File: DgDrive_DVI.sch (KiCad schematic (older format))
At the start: 42 parts, among them J1 Curr. Mod., J2 DVI-I, J3 Ld+, J4 Ld-, J5 Pz+, J6 Pz-, J7 Piezo_In, K1 G6AU, Q1 MMBT3904, Q2 2N4401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

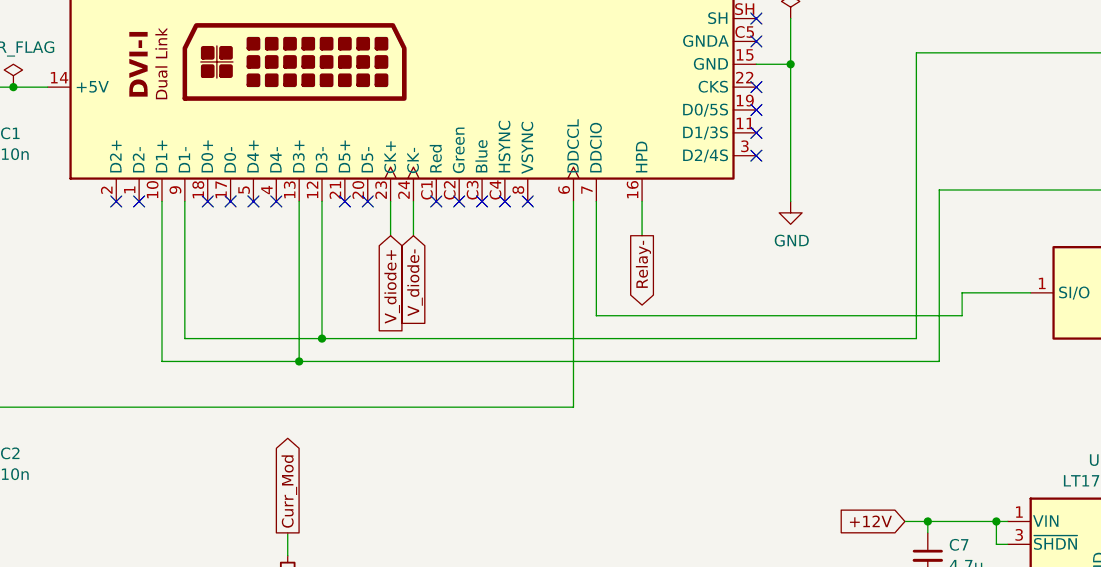
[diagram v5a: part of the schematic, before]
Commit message: Fix laser diode polarity
Switch LD-/LD+ pins at the DVI connector
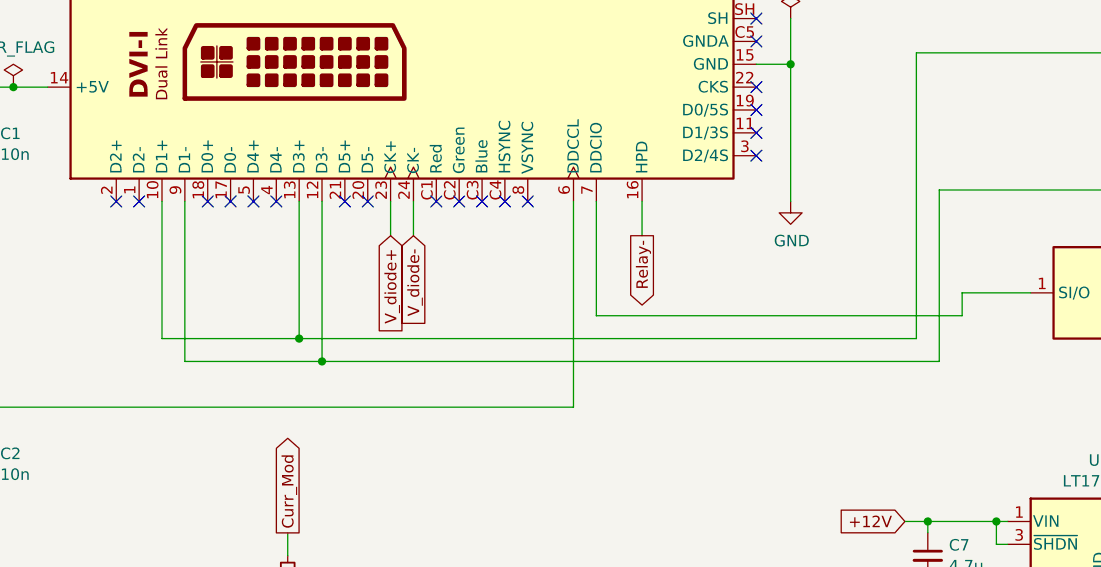
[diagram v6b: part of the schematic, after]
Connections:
- net at J2.10 (D1+), J2.13 (D3+): now also L1.1, R1.2; no longer L2.1, R6.2
- net at J2.12 (D3-), J2.9 (D1-): now also L2.1, R6.2; no longer L1.1, R1.2
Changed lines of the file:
@@
 Sheet 1 1
 Title "Laser Backplane Diode DVI"
-Date "2021-03-15"
-Rev "1.4"
+Date "2021-07-23"
+Rev "1.5"
 Comp "APQ"
 Comment1 "Tilman Preuschoff & Patrick Baus"
@@
 	8650 4200 8650 4100
 Connection ~ 8650 4100
-Wire Wire Line
-	2650 4150 2650 4850
-Wire Wire Line
-	2650 4850 3250 4850
-Wire Wire Line
-	3250 4150 3250 4850
-Connection ~ 3250 4850
-Wire Wire Line
-	2750 4150 2750 4750
-Wire Wire Line
-	2750 4750 3350 4750
-Wire Wire Line
-	3350 4150 3350 4750
-Connection ~ 3350 4750
 NoConn ~ 2450 4150
 NoConn ~ 2550 4150
@@
 	5950 4750 5950 3500
 Wire Wire Line
-	3350 4750 5950 4750
-Wire Wire Line
 	5950 3500 7700 3500
 Wire Wire Line
 	6050 4850 6050 4100
-Wire Wire Line
-	3250 4850 6050 4850
 Wire Wire Line
 	6050 4100 7700 4100
@@
 	1    0    0    1
 $EndComp
+Wire Wire Line
+	3250 4150 3250 4750
+Connection ~ 3250 4750
+Wire Wire Line
+	3250 4750 5950 4750
+Wire Wire Line
+	3350 4150 3350 4850
+Connection ~ 3350 4850
+Wire Wire Line
+	3350 4850 6050 4850
+Wire Wire Line
+	2650 4150 2650 4750
+Wire Wire Line
+	2650 4750 3250 4750
+Wire Wire Line
+	2750 4150 2750 4850
+Wire Wire Line
+	2750 4850 3350 4850
 $EndSCHEMATC

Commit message: Replace XGL3530 with XGL5050
-Use a larger inductance
-Options for no inductance at LD- and ground referenced design.
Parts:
- added JP1: No_L, Jumper:SolderJumper-2_P1.3mm_Open_RoundedPad1.0x1.5mm, symbol Device:Jumper_NO_Small
- added JP2: GND, Jumper:SolderJumper-2_P1.3mm_Open_RoundedPad1.0x1.5mm, symbol Device:Jumper_NO_Small
- C4: MFN (none) -> Yageo; PN (none) -> CC0603CPNPO9BN1R5
- L1: value 3.3u -> 33u; footprint custom:Coilcraft_XGL3530 -> custom:Coilcraft_XGL5050; PN XGL3530-332MEC -> XGL5050-333MEC
- L2: value 3.3u -> 33u; footprint custom:Coilcraft_XGL3530 -> custom:Coilcraft_XGL5050; PN XGL3530-332MEC -> XGL3530-333MEC
- R1, R6: MFN (none) -> Susumu; PN (none) -> RR0816Q-49R9-D-68R
- R4: MFN (none) -> Susumu; PN (none) -> RR0816Q-100-D
- RN1: value 10k -> 1k; PN MORNTA1002AT5 -> MORNTA1001AT5
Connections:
- net GND: now also JP2.2
- net LD_short-: now also JP1.1, JP2.1
- net at J2.12 (D3-), J2.9 (D1-), L2.1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: now also JP1.2
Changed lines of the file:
@@
 F 2 "Resistor_SMD:R_0603_1608Metric" H 8050 3500 50  0001 C CNN
 F 3 "~" H 8050 3500 50  0001 C CNN
-F 4 "" V 8050 3500 50  0001 C CNN "MFN"
-F 5 "" V 8050 3500 50  0001 C CNN "MFP"
+F 4 "Susumu" V 8050 3500 50  0001 C CNN "MFN"
+F 5 "RR0816Q-49R9-D-68R" V 8050 3500 50  0001 C CNN "PN"
 	1    8050 3500
 	0    1    1    0
@@
 F 2 "Resistor_SMD:R_0603_1608Metric" H 8050 4100 50  0001 C CNN
 F 3 "~" H 8050 4100 50  0001 C CNN
-F 4 "" V 8050 4100 50  0001 C CNN "MFN"
-F 5 "" V 8050 4100 50  0001 C CNN "MFP"
+F 4 "Susumu" V 8050 4100 50  0001 C CNN "MFN"
+F 5 "RR0816Q-49R9-D-68R" V 8050 4100 50  0001 C CNN "PN"
 	1    8050 4100
 	0    1    1    0
@@
 P 8050 3200
 F 0 "L1" V 8235 3200 50  0000 C CNN
-F 1 "3.3u" V 8144 3200 50  0000 C CNN
-F 2 "custom:Coilcraft_XGL3530" H 8050 3200 50  0001 C CNN
+F 1 "33u" V 8144 3200 50  0000 C CNN
+F 2 "custom:Coilcraft_XGL5050" H 8050 3200 50  0001 C CNN
 F 3 "~" H 8050 3200 50  0001 C CNN
 F 4 "Coilcraft" V 8050 3200 50  0001 C CNN "MFN"
-F 5 "XGL3530-332MEC" V 8050 3200 50  0001 C CNN "PN"
+F 5 "XGL5050-333MEC" V 8050 3200 50  0001 C CNN "PN"
 	1    8050 3200
 	0    -1   -1   0
@@
 P 8050 4400
 F 0 "L2" V 8235 4400 50  0000 C CNN
-F 1 "3.3u" V 8144 4400 50  0000 C CNN
-F 2 "custom:Coilcraft_XGL3530" H 8050 4400 50  0001 C CNN
+F 1 "33u" V 8144 4400 50  0000 C CNN
+F 2 "custom:Coilcraft_XGL5050" H 8050 4400 50  0001 C CNN
 F 3 "~" H 8050 4400 50  0001 C CNN
 F 4 "Coilcraft" V 8050 4400 50  0001 C CNN "MFN"
-F 5 "XGL3530-332MEC" V 8050 4400 50  0001 C CNN "PN"
+F 5 "XGL3530-333MEC" V 8050 4400 50  0001 C CNN "PN"
 	1    8050 4400
 	0    -1   -1   0
@@
 P 2800 6450
 F 0 "RN1" V 2593 6450 50  0000 C CNN
-F 1 "10k" V 2684 6450 50  0000 C CNN
+F 1 "1k" V 2684 6450 50  0000 C CNN
 F 2 "custom:MSOP-8_3x3mm_P0.65mm_mod" V 2720 6450 50  0001 C CNN
 F 3 "~" H 2800 6450 50  0001 C CNN
 F 4 "Vishay" H 2800 6450 50  0001 C CNN "MFN"
-F 5 "MORNTA1002AT5" H 2800 6450 50  0001 C CNN "PN"
+F 5 "MORNTA1001AT5" H 2800 6450 50  0001 C CNN "PN"
 	1    2800 6450
 	0    1    1    0
@@
 P 3700 6000
 F 0 "RN1" V 3493 6000 50  0000 C CNN
-F 1 "10k" V 3584 6000 50  0000 C CNN
+F 1 "1k" V 3584 6000 50  0000 C CNN
 F 2 "custom:MSOP-8_3x3mm_P0.65mm_mod" V 3620 6000 50  0001 C CNN
 F 3 "~" H 3700 6000 50  0001 C CNN
 F 4 "Vishay" H 3700 6000 50  0001 C CNN "MFN"
-F 5 "MORNTA1002AT5" H 3700 6000 50  0001 C CNN "PN"
+F 5 "MORNTA1001AT5" H 3700 6000 50  0001 C CNN "PN"
 	3    3700 6000
 	0    -1   1    0
@@
 P 3700 7050
 F 0 "RN1" V 3493 7050 50  0000 C CNN
-F 1 "10k" V 3584 7050 50  0000 C CNN
+F 1 "1k" V 3584 7050 50  0000 C CNN
 F 2 "custom:MSOP-8_3x3mm_P0.65mm_mod" V 3620 7050 50  0001 C CNN
 F 3 "~" H 3700 7050 50  0001 C CNN
 F 4 "Vishay" H 3700 7050 50  0001 C CNN "MFN"
-F 5 "MORNTA1002AT5" H 3700 7050 50  0001 C CNN "PN"
+F 5 "MORNTA1001AT5" H 3700 7050 50  0001 C CNN "PN"
 	4    3700 7050
 	0    -1   1    0
@@
 P 2800 6800
 F 0 "RN1" V 2593 6800 50  0000 C CNN
-F 1 "10k" V 2684 6800 50  0000 C CNN
+F 1 "1k" V 2684 6800 50  0000 C CNN
 F 2 "custom:MSOP-8_3x3mm_P0.65mm_mod" V 2720 6800 50  0001 C CNN
 F 3 "~" H 2800 6800 50  0001 C CNN
 F 4 "Vishay" H 2800 6800 50  0001 C CNN "MFN"
-F 5 "MORNTA1002AT5" H 2800 6800 50  0001 C CNN "PN"
+F 5 "MORNTA1001AT5" H 2800 6800 50  0001 C CNN "PN"
 	2    2800 6800
 	0    1    1    0
@@
 F 2 "Capacitor_SMD:C_0603_1608Metric" H 3700 7400 50  0001 C CNN
 F 3 "~" H 3700 7400 50  0001 C CNN
+F 4 "Yageo" V 3700 7400 50  0001 C CNN "MFN"
+F 5 "CC0603CPNPO9BN1R5" V 3700 7400 50  0001 C CNN "PN"
 	1    3700 7400
 	0    1    1    0
@@
 F 2 "Resistor_SMD:R_0603_1608Metric" H 3200 5800 50  0001 C CNN
 F 3 "~" H 3200 5800 50  0001 C CNN
-F 4 "" V 3200 5800 50  0001 C CNN "MFN"
-F 5 "" V 3200 5800 50  0001 C CNN "MFP"
+F 4 "Susumu" V 3200 5800 50  0001 C CNN "MFN"
+F 5 "RR0816Q-100-D" V 3200 5800 50  0001 C CNN "PN"
 	1    3200 5800
 	-1   0    0    1
@@
 P 6850 4550
 F 0 "U4" H 6500 4550 50  0000 R CNN
-F 1 "AT21CS11-STXXXX-X" H 6500 4450 50  0000 R CNN
+F 1 "AT21CS11-STXXXX-X" H 6700 4250 50  0000 R CNN
 F 2 "Package_TO_SOT_SMD:SOT-23" H 6850 4550 50  0001 C CNN
 F 3 "https://ww1.microchip.com/downloads/en/DeviceDoc/AT21CS01-AT21CS11-Data-Sheet-DS20005857D.pdf" H 6850 4550 50  0001 C CNN
@@
 Wire Wire Line
 	2750 4850 3350 4850
+$Comp
+L power:GND #PWR0110
+U 1 1 61145C4C
+P 9600 4750
+F 0 "#PWR0110" H 9600 4500 50  0001 C CNN
+F 1 "GND" H 9605 4577 50  0000 C CNN
+F 2 "" H 9600 4750 50  0001 C CNN
+F 3 "" H 9600 4750 50  0001 C CNN
+	1    9600 4750
+	1    0    0    -1
+$EndComp
+$Comp
+L Device:Jumper_NO_Small JP2
+U 1 1 611463F9
+P 9600 4550
+F 0 "JP2" V 9554 4598 50  0000 L CNN
+F 1 "GND" V 9645 4598 50  0000 L CNN
+F 2 "Jumper:SolderJumper-2_P1.3mm_Open_RoundedPad1.0x1.5mm" H 9600 4550 50  0001 C CNN
+F 3 "~" H 9600 4550 50  0001 C CNN
+F 4 "DNF" V 9600 4550 50  0001 C CNN "Config"
+	1    9600 4550
+	0    1    1    0
+$EndComp
+Wire Wire Line
+	9600 4750 9600 4650
+Wire Wire Line
+	9600 4450 9600 4100
+$Comp
+L Device:Jumper_NO_Small JP1
+U 1 1 61163CD2
+P 8050 4650
+F 0 "JP1" H 8050 4465 50  0000 C CNN
+F 1 "No_L" H 8050 4556 50  0000 C CNN
+F 2 "Jumper:SolderJumper-2_P1.3mm_Open_RoundedPad1.0x1.5mm" H 8050 4650 50  0001 C CNN
+F 3 "~" H 8050 4650 50  0001 C CNN
+F 4 "DNF" V 8050 4650 50  0001 C CNN "Config"
+	1    8050 4650
+	-1   0    0    1
+$EndComp
+Wire Wire Line
+	8150 4650 8450 4650
+Wire Wire Line
+	8450 4650 8450 4400
+Connection ~ 8450 4400
+Wire Wire Line
+	7950 4650 7700 4650
+Wire Wire Line
+	7700 4650 7700 4400
+Connection ~ 7700 4400
 $EndSCHEMATC

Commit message: Remove L2
Remove inductance and bypass resistor at Ld-.
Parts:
- removed JP1: No_L, Jumper:SolderJumper-2_P1.3mm_Open_RoundedPad1.0x1.5mm, symbol Device:Jumper_NO_Small
- removed L2: 33u, custom:Coilcraft_XGL5050, symbol Device:L_Small
- removed R6: 49.9, Resistor_SMD:R_0603_1608Metric, symbol Device:R_Small
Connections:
- net LD_short-: now also J2.12 (D3-), J2.9 (D1-)
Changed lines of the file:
@@
 Sheet 1 1
 Title "Laser Backplane Diode DVI"
-Date "2021-07-23"
-Rev "1.5"
+Date "2021-10-07"
+Rev "1.6"
 Comp "APQ"
 Comment1 "Tilman Preuschoff & Patrick Baus"
@@
 $EndComp
 Wire Wire Line
-	7950 4100 7700 4100
-Wire Wire Line
 	7950 3500 7700 3500
-$Comp
-L Device:R_Small R6
-U 1 1 5DF25AA7
-P 8050 4100
-F 0 "R6" V 7854 4100 50  0000 C CNN
-F 1 "49.9" V 7945 4100 50  0000 C CNN
-F 2 "Resistor_SMD:R_0603_1608Metric" H 8050 4100 50  0001 C CNN
-F 3 "~" H 8050 4100 50  0001 C CNN
-F 4 "Susumu" V 8050 4100 50  0001 C CNN "MFN"
-F 5 "RR0816Q-49R9-D-68R" V 8050 4100 50  0001 C CNN "PN"
-	1    8050 4100
-	0    1    1    0
-$EndComp
 Text GLabel 3650 4300 3    50   Input ~ 0
 V_diode+
@@
 	1    0    0    -1
 $EndComp
-Wire Wire Line
-	8150 4100 8450 4100
 Wire Wire Line
 	9300 3800 9250 3800
@@
 	0    -1   -1   0
 $EndComp
-$Comp
-L Device:L_Small L2
-U 1 1 604BF8B4
-P 8050 4400
-F 0 "L2" V 8235 4400 50  0000 C CNN
-F 1 "33u" V 8144 4400 50  0000 C CNN
-F 2 "custom:Coilcraft_XGL5050" H 8050 4400 50  0001 C CNN
-F 3 "~" H 8050 4400 50  0001 C CNN
-F 4 "Coilcraft" V 8050 4400 50  0001 C CNN "MFN"
-F 5 "XGL3530-333MEC" V 8050 4400 50  0001 C CNN "PN"
-	1    8050 4400
-	0    -1   -1   0
-$EndComp
-Wire Wire Line
-	8150 4400 8450 4400
-Wire Wire Line
-	8450 4400 8450 4100
-Connection ~ 8450 4100
-Wire Wire Line
-	8450 4100 8650 4100
-Wire Wire Line
-	7950 4400 7700 4400
-Wire Wire Line
-	7700 4400 7700 4100
-Connection ~ 7700 4100
 Wire Wire Line
 	8450 3200 8450 3500
@@
 Wire Wire Line
 	6050 4850 6050 4100
-Wire Wire Line
-	6050 4100 7700 4100
 Text GLabel 9600 3000 1    50   Input ~ 0
 Curr_Mod
@@
 Wire Wire Line
 	9600 4450 9600 4100
-$Comp
-L Device:Jumper_NO_Small JP1
-U 1 1 61163CD2
-P 8050 4650
-F 0 "JP1" H 8050 4465 50  0000 C CNN
-F 1 "No_L" H 8050 4556 50  0000 C CNN
-F 2 "Jumper:SolderJumper-2_P1.3mm_Open_RoundedPad1.0x1.5mm" H 8050 4650 50  0001 C CNN
-F 3 "~" H 8050 4650 50  0001 C CNN
-F 4 "DNF" V 8050 4650 50  0001 C CNN "Config"
-	1    8050 4650
-	-1   0    0    1
-$EndComp
-Wire Wire Line
-	8150 4650 8450 4650
-Wire Wire Line
-	8450 4650 8450 4400
-Connection ~ 8450 4400
-Wire Wire Line
-	7950 4650 7700 4650
-Wire Wire Line
-	7700 4650 7700 4400
-Connection ~ 7700 4400
+Wire Wire Line
+	6050 4100 8650 4100
 $EndSCHEMATC
